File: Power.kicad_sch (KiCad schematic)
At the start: 55 parts, among them J1 A, J2 B, J3 C, Q1 2N7002, Q2 2N7002, Q3 2N7002, Q4 2N7002, Q5 2N7002, Q6 2N7002

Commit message: Первый вариант
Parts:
- added C46, C47, C48, C49, C50, C51: 10u, Capacitor_SMD:C_1206_3216Metric_Pad1.33x1.80mm_HandSolder, symbol Device:C_Small
- added R3: PU2512FKGP60U5L, Resistor_SMD:R_2512_6332Metric_Pad1.40x3.35mm_HandSolder, symbol Device:R
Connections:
- net +24V: now also R3.1
- net GND: now also C46.2, C47.2, C48.2, C49.2, C50.2, C51.2
- net Shunt_2 renamed Shunt-
- net Shunt-: now also C46.1, C47.1, C48.1, C49.1, C50.1, C51.1, R3.2

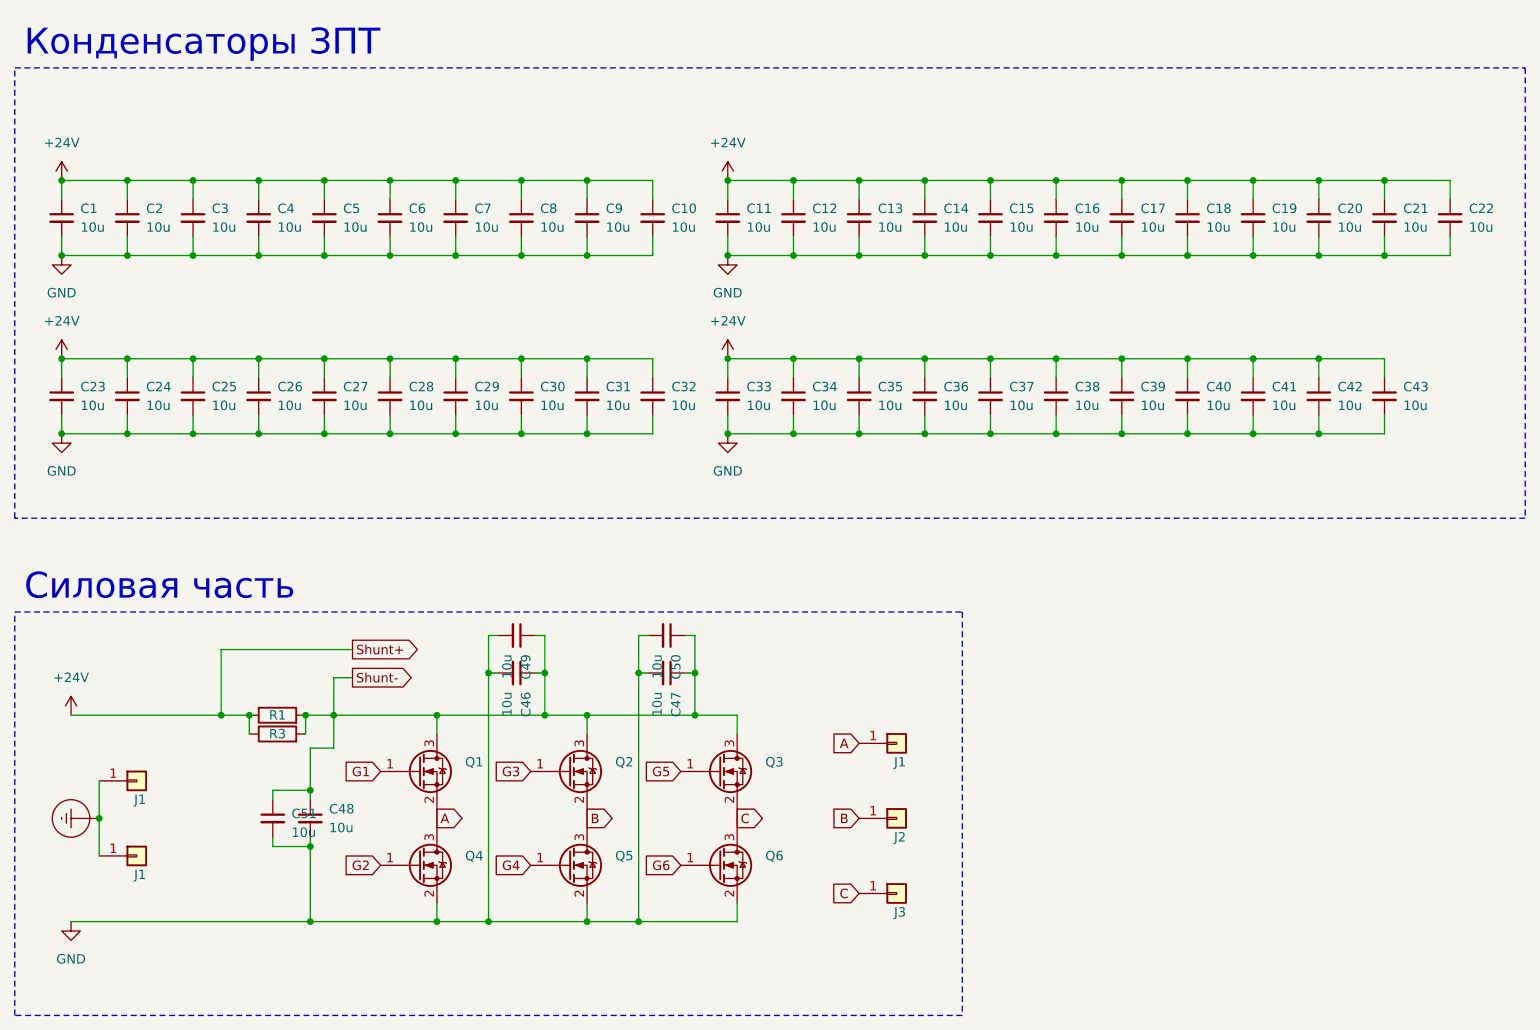
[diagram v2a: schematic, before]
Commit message: Заменил разъёмы 2.54 на 1.27мм
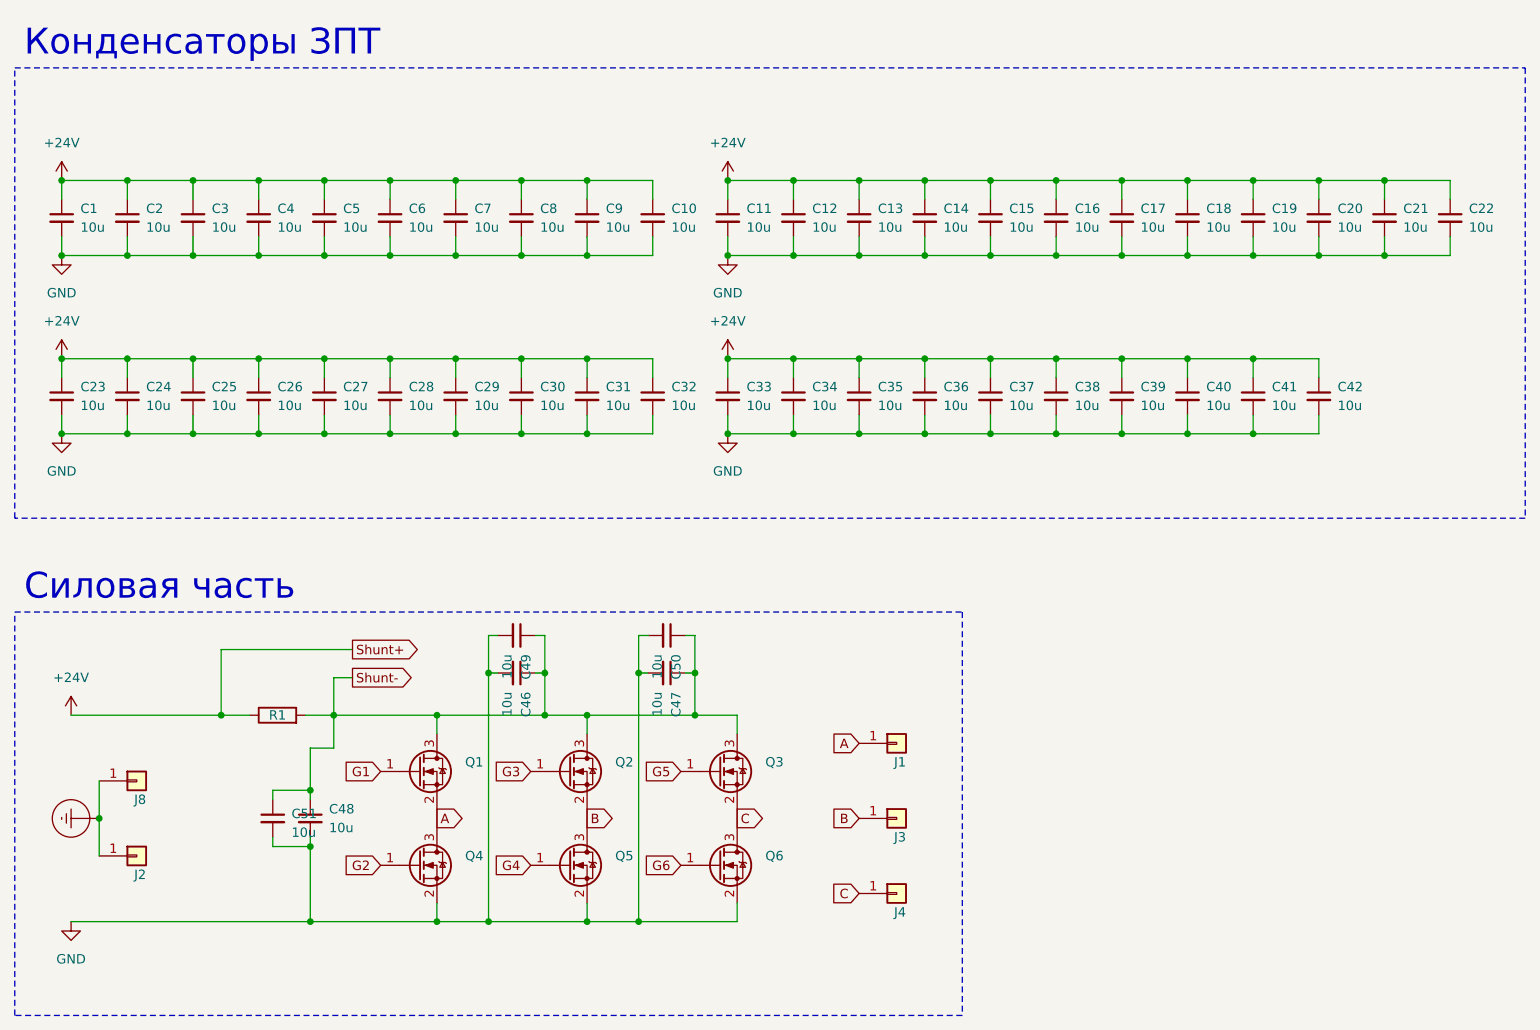
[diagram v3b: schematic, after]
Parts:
- removed C43: 10u, Capacitor_SMD:C_1210_3225Metric_Pad1.33x2.70mm_HandSolder, symbol Device:C_Small
- removed R3: PU2512FKGP60U5L, Resistor_SMD:R_2512_6332Metric_Pad1.40x3.35mm_HandSolder, symbol Device:R
- renumbered J1 to J2, J2 to J3, J3 to J4, J1 to J8

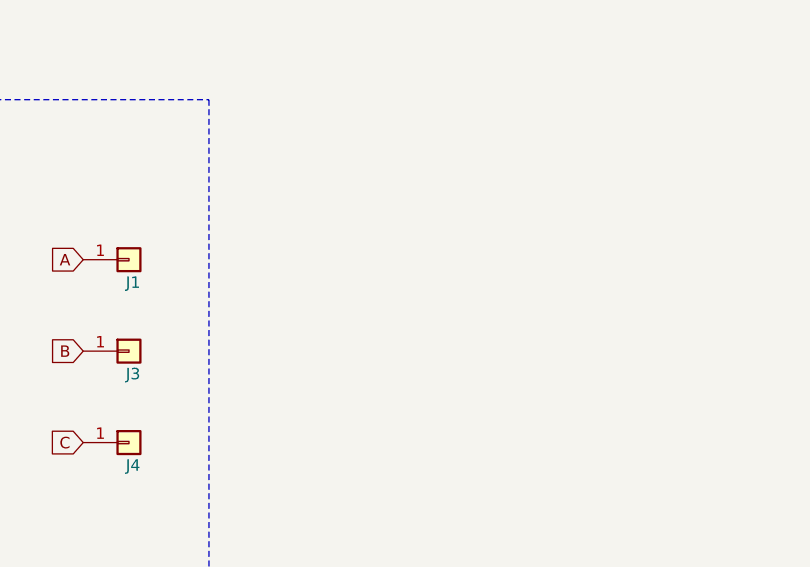
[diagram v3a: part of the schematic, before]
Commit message: Добавил подтяжки затворов на плату
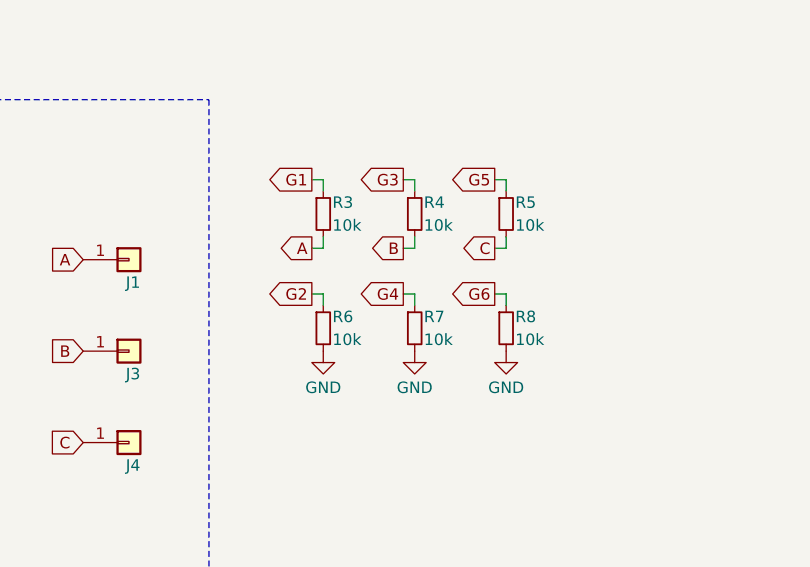
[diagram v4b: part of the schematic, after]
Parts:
- added R3, R4, R5, R6, R7, R8: 10k, Resistor_SMD:R_0603_1608Metric_Pad0.98x0.95mm_HandSolder, symbol Device:R_Small
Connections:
- net A: now also R3.2
- net B: now also R4.2
- net C: now also R5.2
- net G1: now also R3.1
- net G2: now also R6.1
- net G3: now also R4.1
- net G4: now also R7.1
- net G5: now also R5.1
- net G6: now also R8.1
- net GND: now also R6.2, R7.2, R8.2
